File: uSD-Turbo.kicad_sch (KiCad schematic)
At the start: 14 parts, among them J1 User Port, U1 74LVC125AD, U2 AMS1117-3.3

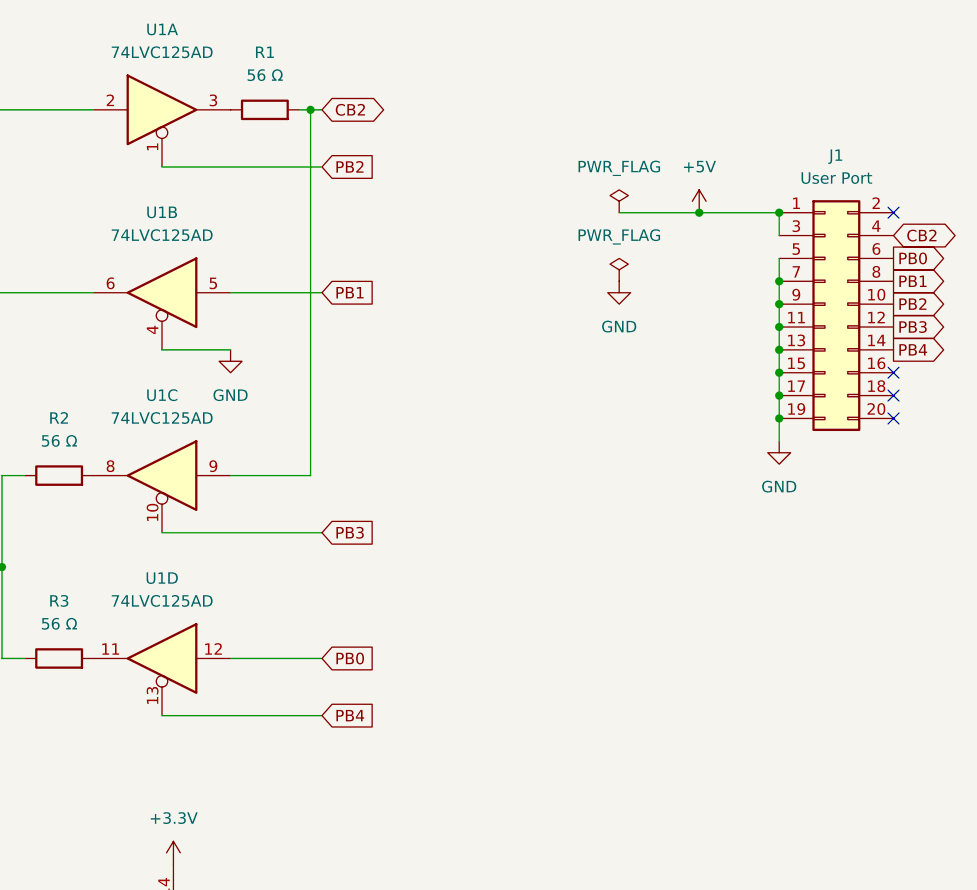
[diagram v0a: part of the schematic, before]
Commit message: Renamed project, added resistor between PB1 and CB1, added BOM and Gerber files
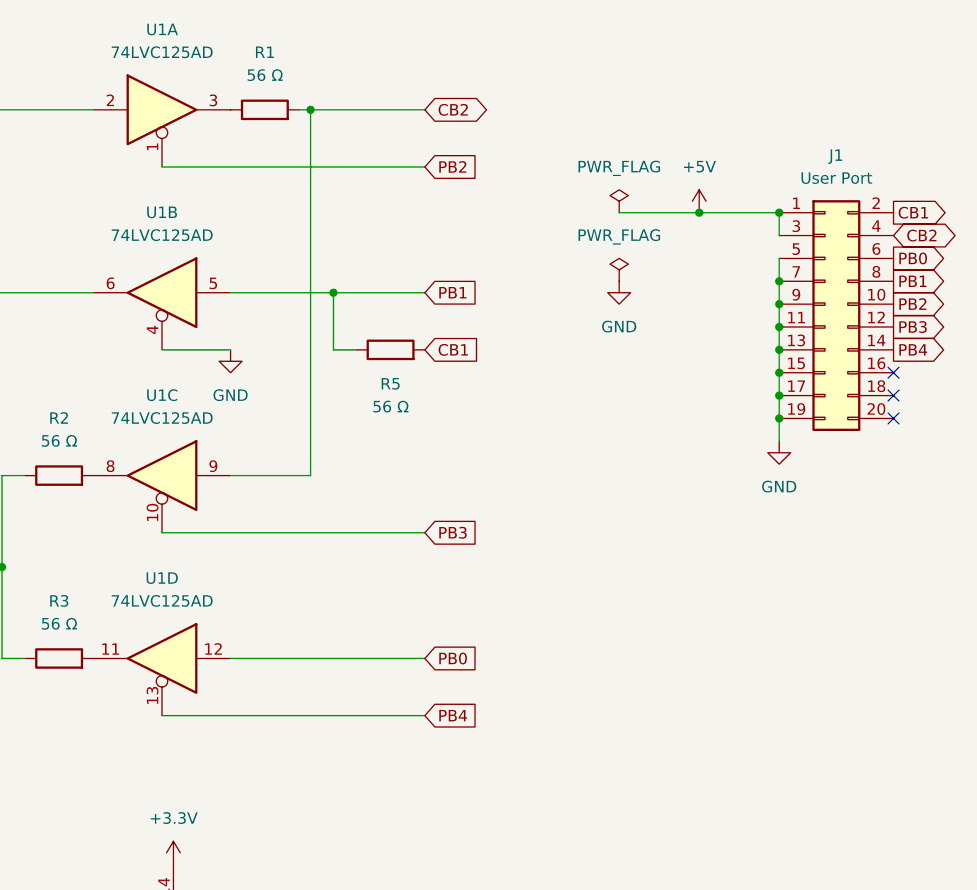
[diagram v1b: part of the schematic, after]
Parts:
- added R5: 56 Ω, Resistor_SMD:R_0603_1608Metric, symbol Device:R
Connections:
- net PB1: now also R5.1
- net CB1: now reaches J1.2 (Pin_2)
- net CB1: now also R5.2
- no-connect marks 7 -> 6
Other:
- company: (none) -> J. Hilsdorf
- title: (none) -> µSD Turbo 1.0
